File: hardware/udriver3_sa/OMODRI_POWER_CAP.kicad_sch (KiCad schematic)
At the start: 20 parts

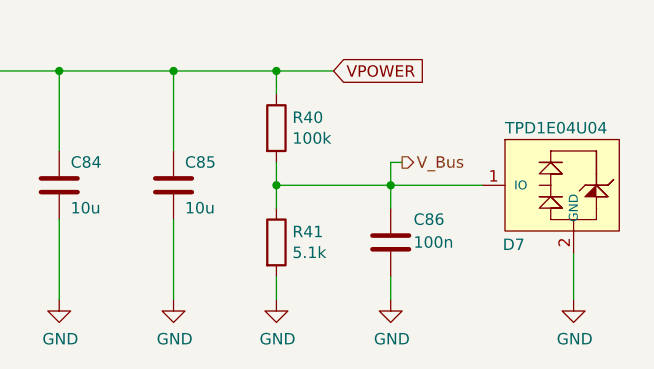
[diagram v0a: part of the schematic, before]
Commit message: Third release of uOmodri Single Axis (uOmodri_SA). Add Test points.
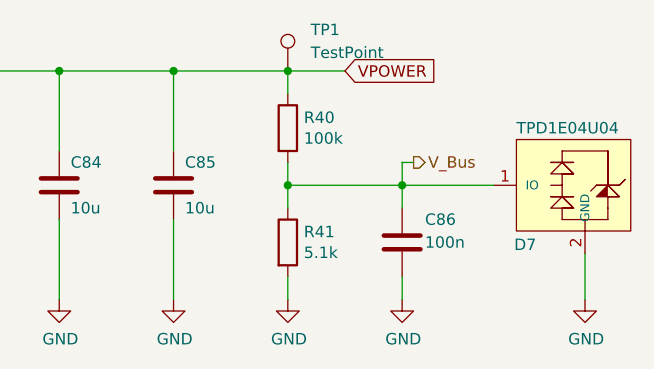
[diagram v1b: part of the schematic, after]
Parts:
- added TP1: TestPoint, TestPoint:TestPoint_Pad_D1.0mm, symbol Connector:TestPoint
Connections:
- net VPOWER: now also TP1.1
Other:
- moved on the sheet: C86, D7, R40, R41

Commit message: Update some reference on uOmodri V3.1 for fab. Update uOmodri_SA V1.0 reducing heights of top layers components.
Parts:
- C70, C71, C72, C73, C74, C75: value 10u -> 4.7u; footprint Capacitor_SMD:C_1210_3225Metric -> Capacitor_SMD:C_1206_3216Metric; DigiKey 490-16266-1-ND -> 490-18620-1-ND; Farnell 3581425 -> 3790450; LCSC C576517 -> C237304; Mouser 81-GRM32EC72A106KE05 -> 81-GRM31CC72A475KE1L; Part No GRM32EC72A106KE05L -> GRM31CC72A475KE11#; RS 247-8166 -> 2478147

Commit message: Update on uOmodri_SA. Remove USB, com SPI & debug connectors for integration into Myactuator motors. Connectors replaced by a ZIF connector.
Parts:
- renumbered C70 to C71, C71 to C72, C72 to C73, C73 to C74, C74 to C75, C75 to C76, C76 to C77, C77 to C78, C78 to C79, C79 to C80, C80 to C81, C81 to C82, C82 to C83, C83 to C84, C84 to C85, C85 to C86, C86 to C87, R40 to R38, R41 to R39, TP1 to TP2
